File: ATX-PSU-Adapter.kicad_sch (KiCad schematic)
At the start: 13 parts, among them J1 Conn_02x12_Top_Bottom, J2 Conn_01x06, J3 Conn_01x06, J4 Conn_01x06, J5 Conn_01x06, J6 Conn_01x06, J7 Conn_02x03_Odd_Even, U1 PC817

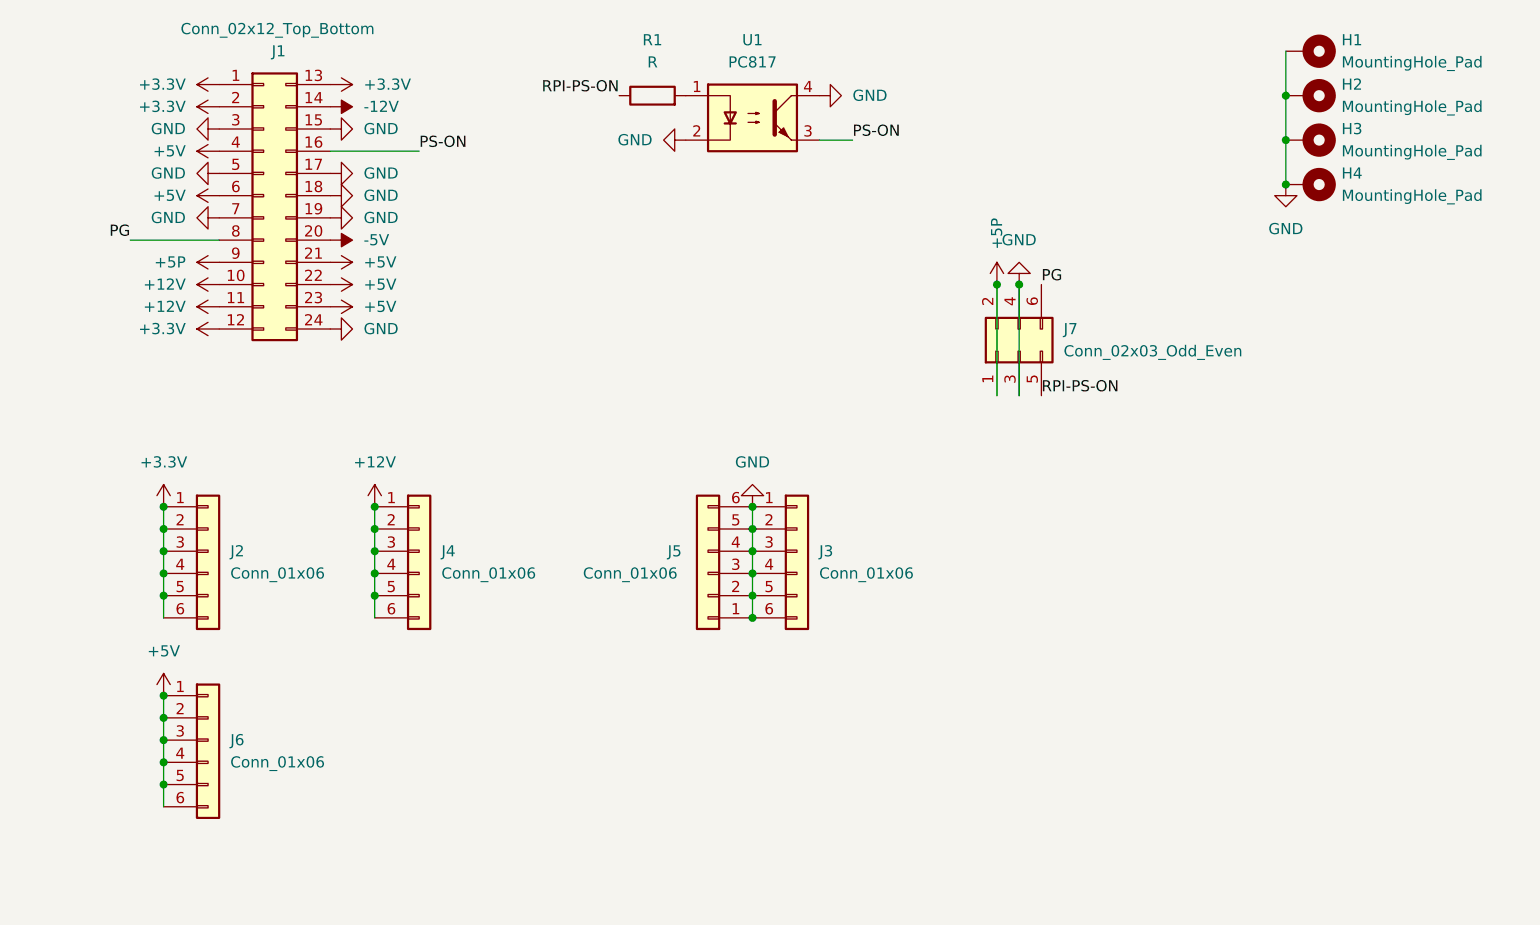
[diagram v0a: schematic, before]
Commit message: Replace ATX Connector
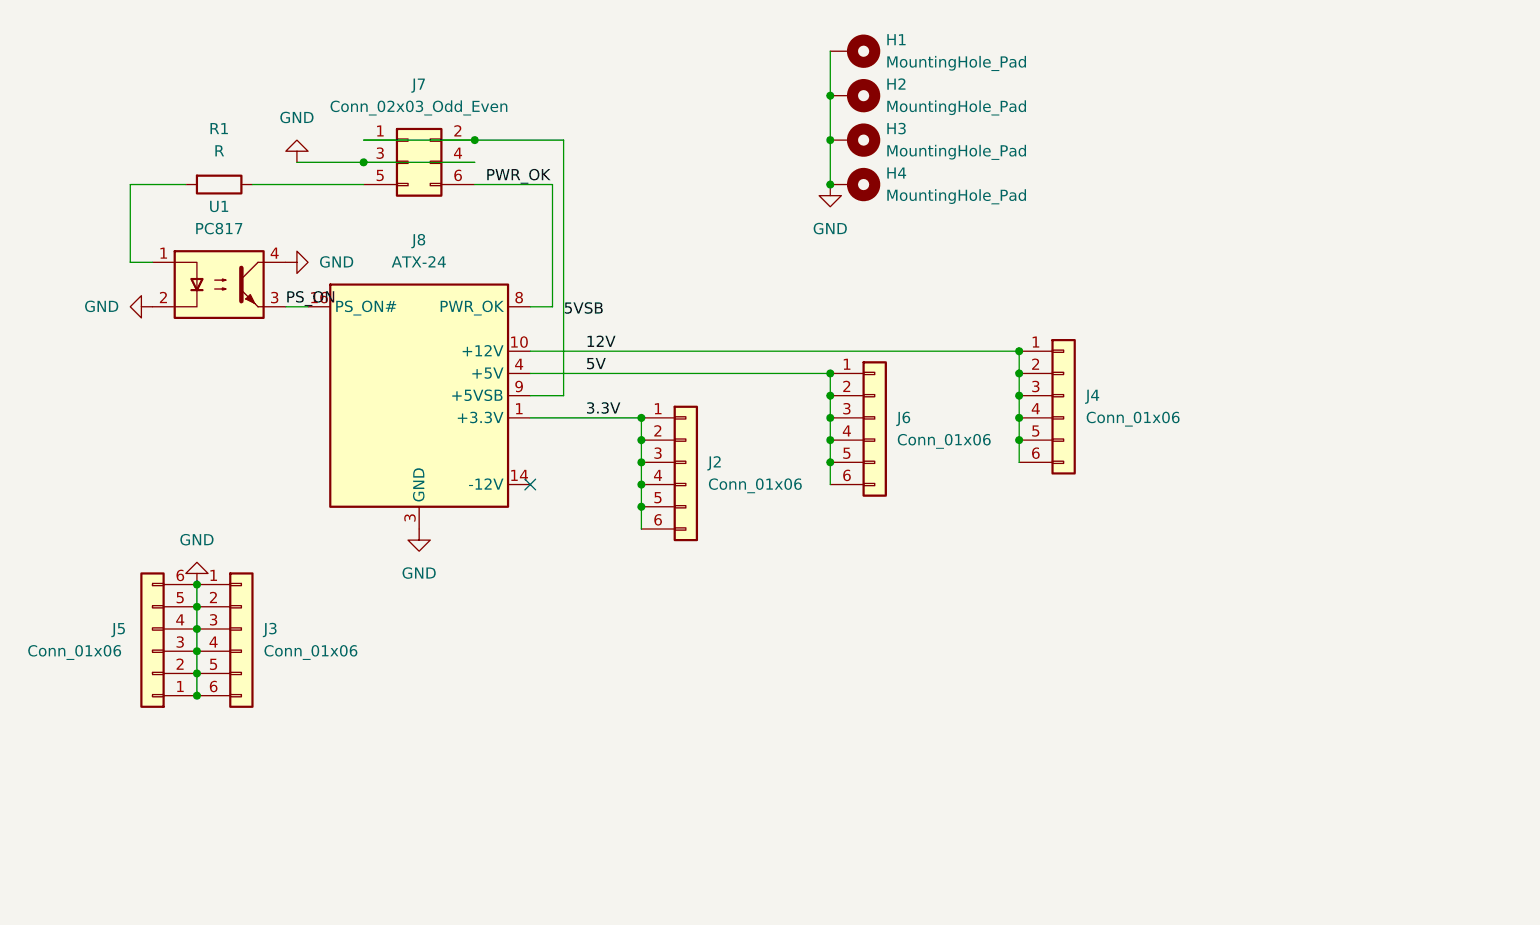
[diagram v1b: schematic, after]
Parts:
- removed J1: Conn_02x12_Top_Bottom, Connector_Molex:Molex_Mini-Fit_Jr_5566-24A_2x12_P4.20mm_Vertical, symbol Connector_Generic:Conn_02x12_Top_Bottom
- added J8: ATX-24, Connector_Molex:Molex_Mini-Fit_Jr_5566-24A_2x12_P4.20mm_Vertical, symbol Connector:ATX-24
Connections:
- net GND: now also J8.15 (GND), J8.17 (GND), J8.18 (GND), J8.19 (GND), J8.24 (GND), J8.3 (GND), J8.5 (GND), J8.7 (GND)
- net +12V renamed 12V
- net 12V: now also J8.10 (+12V), J8.11 (+12V)
- net +3.3V renamed 3.3V
- net 3.3V: now also J8.1 (+3.3V), J8.12 (+3.3V), J8.13 (+3.3V), J8.2 (+3.3V)
- net +5P renamed 5VSB
- net 5VSB: now also J8.9 (+5VSB)
- net +5V renamed 5V
- net 5V: now also J8.21 (+5V), J8.22 (+5V), J8.23 (+5V), J8.4 (+5V), J8.6 (+5V)
- net PG renamed PWR_OK
- net PWR_OK: now also J8.8 (PWR_OK)
- net PS-ON renamed PS_ON
- net PS_ON: now also J8.16 (PS_ON#)
- net RPI-PS-ON: no longer names the net of J7.5 (Pin_5), R1.1
- no-connect marks 0 -> 1
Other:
- moved on the sheet: H1, H2, H3, H4, J2, J3, J4, J5, J6, J7, R1, U1

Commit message: Replace pinheader
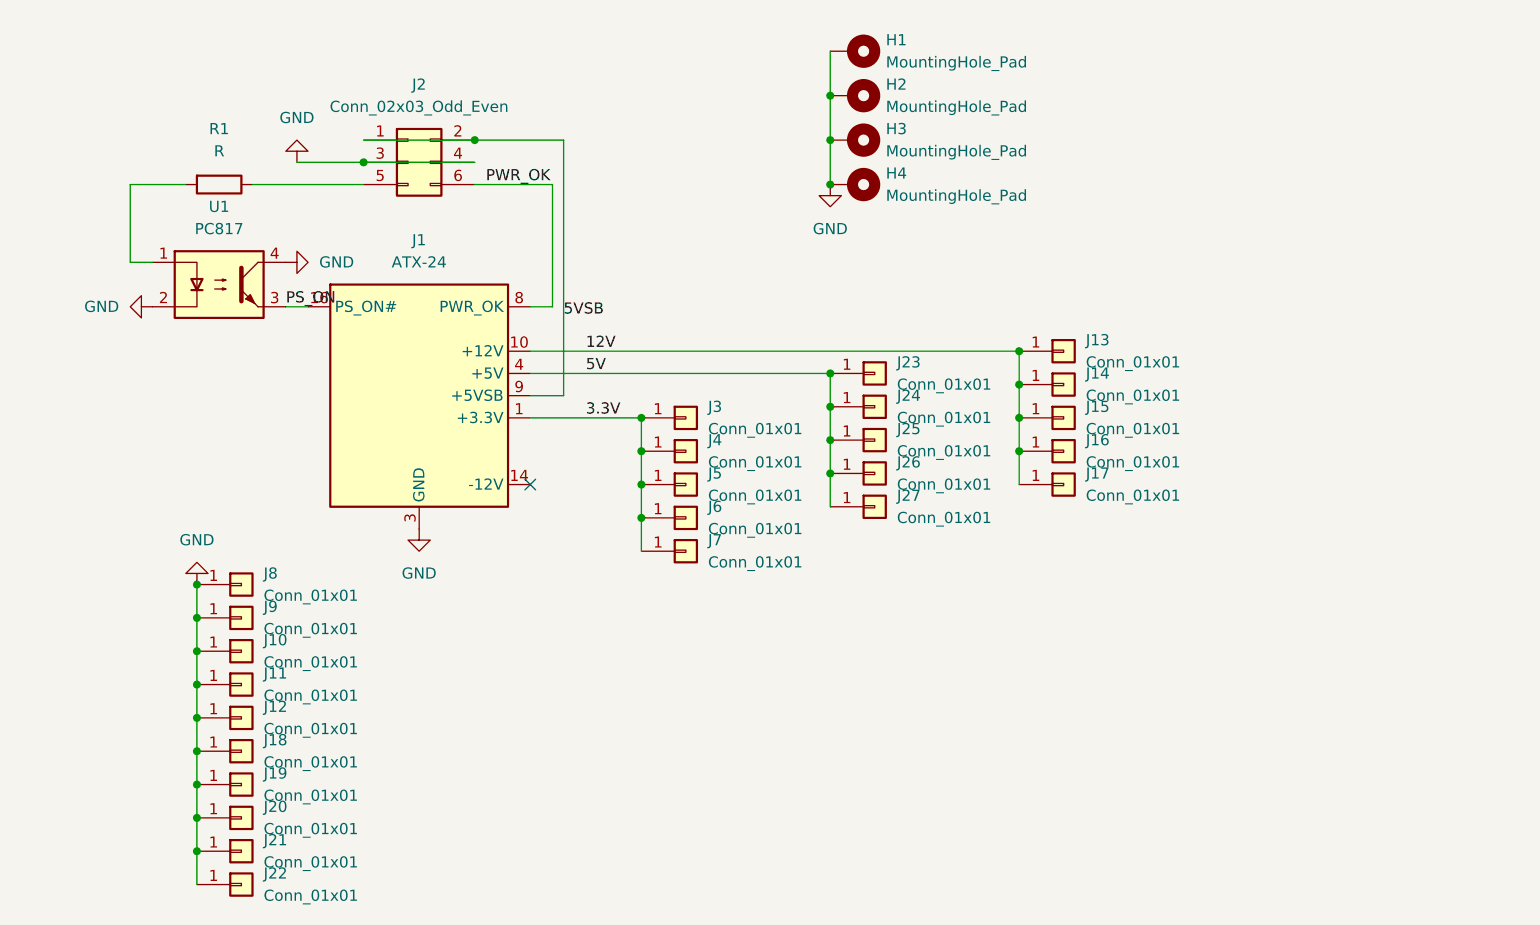
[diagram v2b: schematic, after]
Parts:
- removed J2, J3, J4, J5, J6: Conn_01x06, Connector_PinHeader_2.54mm:PinHeader_1x06_P2.54mm_Vertical, symbol Connector_Generic:Conn_01x06
- added J10, J11, J14, J15, J16, J19, J20, J21, J24, J25, J26, J4, J5, J6, J9: Conn_01x01, Connector_Wire:SolderWire-0.75sqmm_1x01_D1.25mm_OD2.3mm, symbol Connector_Generic:Conn_01x01
- added J12, J17, J22, J27, J7: Conn_01x01, Connector_Wire:SolderWire-1sqmm_1x01_D1.4mm_OD2.7mm, symbol Connector_Generic:Conn_01x01
- added J13, J18, J23, J3, J8: Conn_01x01, Connector_Wire:SolderWire-0.5sqmm_1x01_D0.9mm_OD2.3mm, symbol Connector_Generic:Conn_01x01
- renumbered J8 to J1, J7 to J2
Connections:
- net 12V: now also J13.1 (Pin_1), J14.1 (Pin_1), J15.1 (Pin_1), J16.1 (Pin_1), J17.1 (Pin_1)
- net 3.3V: now also J3.1 (Pin_1), J4.1 (Pin_1), J5.1 (Pin_1), J6.1 (Pin_1), J7.1 (Pin_1)
- net 5V: now also J23.1 (Pin_1), J24.1 (Pin_1), J25.1 (Pin_1), J26.1 (Pin_1), J27.1 (Pin_1)
- net GND: now also J10.1 (Pin_1), J11.1 (Pin_1), J12.1 (Pin_1), J18.1 (Pin_1), J19.1 (Pin_1), J20.1 (Pin_1), J21.1 (Pin_1), J22.1 (Pin_1), J8.1 (Pin_1), J9.1 (Pin_1)

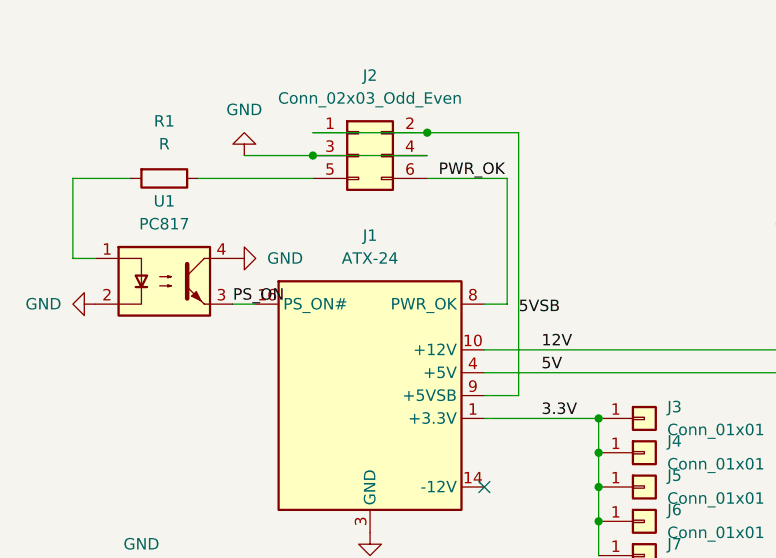
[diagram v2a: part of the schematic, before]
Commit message: Switch 5VSB and GND
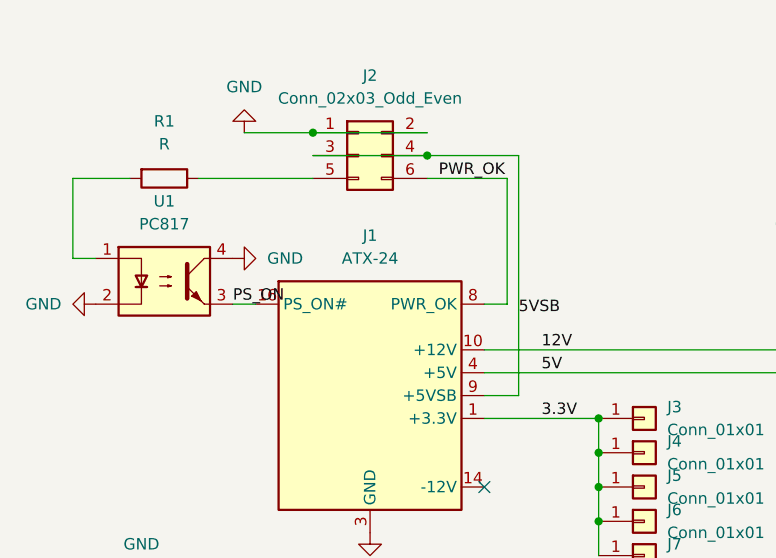
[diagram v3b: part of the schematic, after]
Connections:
- net 5VSB: now also J2.3 (Pin_3), J2.4 (Pin_4); no longer J2.1 (Pin_1), J2.2 (Pin_2)
- net GND: now also J2.1 (Pin_1), J2.2 (Pin_2); no longer J2.3 (Pin_3), J2.4 (Pin_4)
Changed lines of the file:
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@@
   (junction (at 107.95 59.69) (diameter 0) (color 0 0 0 0)
   )
-  (junction (at 54.61 35.56) (diameter 0) (color 0 0 0 0)
+  (junction (at 54.61 33.02) (diameter 0) (color 0 0 0 0)
   )
   (junction (at 107.95 33.02) (diameter 0) (color 0 0 0 0)
@@
   (junction (at 35.56 87.63) (diameter 0) (color 0 0 0 0)
   )
-  (junction (at 67.31 33.02) (diameter 0) (color 0 0 0 0)
-  )
   (junction (at 107.95 63.5) (diameter 0) (color 0 0 0 0)
   )
@@
   )
   (junction (at 86.36 68.58) (diameter 0) (color 0 0 0 0)
+  )
+  (junction (at 67.31 35.56) (diameter 0) (color 0 0 0 0)
   )
   (junction (at 107.95 67.31) (diameter 0) (color 0 0 0 0)
@@
     (stroke (width 0) (type default))
   )
-  (wire (pts (xy 46.99 35.56) (xy 54.61 35.56))
-    (stroke (width 0) (type default))
-  )
   (wire (pts (xy 86.36 72.39) (xy 86.36 76.2))
     (stroke (width 0) (type default))
@@
     (stroke (width 0) (type default))
   )
+  (wire (pts (xy 77.47 35.56) (xy 67.31 35.56))
+    (stroke (width 0) (type default))
+  )
   (wire (pts (xy 35.56 106.68) (xy 35.56 110.49))
     (stroke (width 0) (type default))
@@
     (stroke (width 0) (type default))
   )
-  (wire (pts (xy 67.31 33.02) (xy 77.47 33.02))
+  (wire (pts (xy 46.99 33.02) (xy 54.61 33.02))
     (stroke (width 0) (type default))
   )
@@
     (stroke (width 0) (type default))
   )
+  (wire (pts (xy 77.47 62.23) (xy 77.47 35.56))
+    (stroke (width 0) (type default))
+  )
   (wire (pts (xy 107.95 22.86) (xy 107.95 27.94))
     (stroke (width 0) (type default))
@@
   )
   (wire (pts (xy 67.31 38.1) (xy 76.2 38.1))
-    (stroke (width 0) (type default))
-  )
-  (wire (pts (xy 77.47 62.23) (xy 77.47 33.02))
     (stroke (width 0) (type default))
   )
@@
     )
   )
-  (symbol (lib_id "power:GND") (at 46.99 35.56 180) (unit 1)
-    (in_bom yes) (on_board yes) (dnp no) (fields_autoplaced)
-    (property "Reference" "#PWR030" (at 46.99 29.21 0)
-      (effects (font (size 1.27 1.27)) hide)
-    )
-    (property "Value" "GND" (at 46.99 30.48 0)
+  (symbol (lib_id "power:GND") (at 46.99 33.02 180) (unit 1)
+    (in_bom yes) (on_board yes) (dnp no) (fields_autoplaced)
+    (property "Reference" "#PWR030" (at 46.99 26.67 0)
+      (effects (font (size 1.27 1.27)) hide)
+    )
+    (property "Value" "GND" (at 46.99 27.94 0)
       (effects (font (size 1.27 1.27)))
     )
-    (property "Footprint" "" (at 46.99 35.56 0)
-      (effects (font (size 1.27 1.27)) hide)
-    )
-    (property "Datasheet" "" (at 46.99 35.56 0)
-      (effects (font (size 1.27 1.27)) hide)
-    )
+    (property "Footprint" "" (at 46.99 33.02 0)
+      (effects (font (size 1.27 1.27)) hide)
+    )
+    (property "Datasheet" "" (at 46.99 33.02 0)
+      (effects (font (size 1.27 1.27)) hide)
+    )

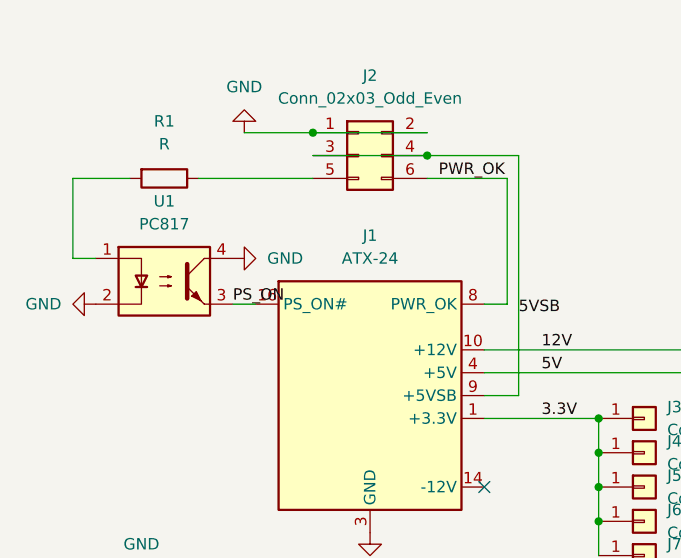
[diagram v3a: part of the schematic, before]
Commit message: Fix: ATX Connector Footprint, Optocoupler wiring
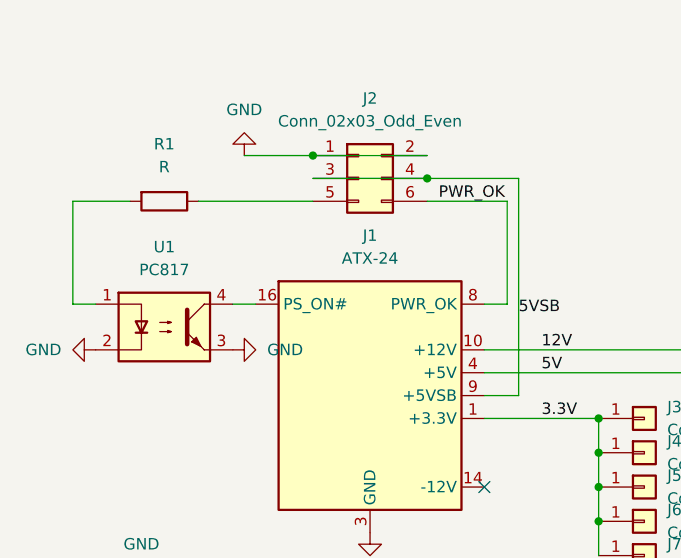
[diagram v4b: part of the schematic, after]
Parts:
- J1: footprint Connector_Molex:Molex_Mini-Fit_Jr_5566-24A_2x12_P4.20mm_Vertical -> Connector_Molex_Mod:Molex_Mod_Mini-Fit_Jr_5566-24A_2x12_P4.20mm_Vertical
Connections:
- net GND: now also U1.3; no longer U1.4
- net PS_ON: no longer names the net of J1.16 (PS_ON#)
- net PS_ON: now also U1.4; no longer U1.3
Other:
- moved on the sheet: J2, R1, U1

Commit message: Replace ATX connector, wiring and layout
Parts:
- J1: footprint Connector_Molex_Mod:Molex_Mod_Mini-Fit_Jr_5566-24A_2x12_P4.20mm_Vertical -> Connector_Molex:Molex_Mini-Fit_Jr_5566-24A_2x12_P4.20mm_Vertical
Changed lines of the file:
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@@
       (effects (font (size 1.27 1.27)))
     )
-    (property "Footprint" "Connector_Molex_Mod:Molex_Mod_Mini-Fit_Jr_5566-24A_2x12_P4.20mm_Vertical" (at 60.96 64.77 0)
+    (property "Footprint" "Connector_Molex:Molex_Mini-Fit_Jr_5566-24A_2x12_P4.20mm_Vertical" (at 60.96 64.77 0)
       (effects (font (size 1.27 1.27)) hide)
     )
